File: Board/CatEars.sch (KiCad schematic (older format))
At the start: 41 parts, among them J1 Conn_01x03, J2 USB_B_Micro, J3 Conn_01x03, J31 Conn_01x01, J32 Conn_01x01, SW1 SW_Push, U1 ATSAMD21E18A-AU, U2 AP2112K-3.3

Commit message: Minor board design revision to allow more space to connect battery and easier assembly
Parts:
- removed SW1: SW_Push, Button_Switch_SMD:SW_SPST_EVQPE1, symbol Switch:SW_Push
- added 3V3, GND0: Conn_01x01, TestPoint:TestPoint_Pad_D1.0mm, symbol Connector_Generic:Conn_01x01
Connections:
- net +3V3: now also 3V3.1 (Pin_1)
- net GND: now also GND0.1 (Pin_1)
- no-connect marks 22 -> 23
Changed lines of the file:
@@
-	1    0    0    -1
-$EndComp
-$Comp
-L power:GND #PWR0103
-U 1 1 5E1A21AD
-P 5100 2350
-F 0 "#PWR0103" H 5100 2100 50  0001 C CNN
-F 1 "GND" H 5105 2177 50  0000 C CNN
-F 2 "" H 5100 2350 50  0001 C CNN
-F 3 "" H 5100 2350 50  0001 C CNN
-	1    5100 2350
 	1    0    0    -1
 $EndComp
@@
 F 3 "~" H 4650 1300 50  0001 C CNN
 	1    4650 1300
-	1    0    0    -1
-$EndComp
-$Comp
-L Switch:SW_Push SW1
-U 1 1 5E29FBEB
-P 4900 2350
-F 0 "SW1" H 4900 2635 50  0000 C CNN
-F 1 "SW_Push" H 4900 2544 50  0000 C CNN
-F 2 "Button_Switch_SMD:SW_SPST_EVQPE1" H 4900 2550 50  0001 C CNN
-F 3 "~" H 4900 2550 50  0001 C CNN
-	1    4900 2350
 	1    0    0    -1
 $EndComp
@@
 $EndComp
 Wire Wire Line
-	4350 2350 4700 2350
-Wire Wire Line
 	650  3500 650  3900
 Connection ~ 900  4050
-Connection ~ 900  3750
 Wire Wire Line
 	5300 3900 6350 3900
@@
 Wire Wire Line
 	5850 4050 6000 4050
-Connection ~ 5850 3750
 Wire Wire Line
 	6000 3750 6000 3600
@@
 $EndComp
 $Comp
-L power:+3.3V #PWR0122
-U 1 1 5E42FF29
-P 5850 3750
-F 0 "#PWR0122" H 5850 3600 50  0001 C CNN
-F 1 "+3.3V" H 5865 3923 50  0000 C CNN
-F 2 "" H 5850 3750 50  0001 C CNN
-F 3 "" H 5850 3750 50  0001 C CNN
-	1    5850 3750
-	1    0    0    -1
-$EndComp
-$Comp
 L Device:C C4
 U 1 1 5E42FF1F
@@
 Wire Wire Line
 	4200 4050 4350 4050
-Connection ~ 4200 3750
 Wire Wire Line
 	4350 3750 4350 3600
@@
 $EndComp
 $Comp
-L power:+3.3V #PWR0120
-U 1 1 5E429F5A
-P 4200 3750
-F 0 "#PWR0120" H 4200 3600 50  0001 C CNN
-F 1 "+3.3V" H 4215 3923 50  0000 C CNN
-F 2 "" H 4200 3750 50  0001 C CNN
-F 3 "" H 4200 3750 50  0001 C CNN
-	1    4200 3750
-	1    0    0    -1
-$EndComp
-$Comp
 L Device:C C3
 U 1 1 5E429F50
@@
 Wire Wire Line
 	2550 4050 2700 4050
-Connection ~ 2550 3750
 Wire Wire Line
 	2700 3750 2700 3600
@@
 $EndComp
 $Comp
-L power:+3.3V #PWR0118
-U 1 1 5E420545
-P 2550 3750
-F 0 "#PWR0118" H 2550 3600 50  0001 C CNN
-F 1 "+3.3V" H 2565 3923 50  0000 C CNN
-F 2 "" H 2550 3750 50  0001 C CNN
-F 3 "" H 2550 3750 50  0001 C CNN
-	1    2550 3750
-	1    0    0    -1
-$EndComp
-$Comp
 L Device:C C2
 U 1 1 5E42053B
@@
 $EndComp
 $Comp
-L power:+3.3V #PWR0101
-U 1 1 5E0B2653
-P 900 3750
-F 0 "#PWR0101" H 900 3600 50  0001 C CNN
-F 1 "+3.3V" H 915 3923 50  0000 C CNN
-F 2 "" H 900 3750 50  0001 C CNN
-F 3 "" H 900 3750 50  0001 C CNN
-	1    900  3750
-	1    0    0    -1
-$EndComp
-$Comp
 L Device:C C1
 U 1 1 5E0B059C
@@
 $EndComp
 $Comp
-L power:+3.3V #PWR0124
-U 1 1 5E43570B
-P 7500 3750
-F 0 "#PWR0124" H 7500 3600 50  0001 C CNN
-F 1 "+3.3V" H 7515 3923 50  0000 C CNN
-F 2 "" H 7500 3750 50  0001 C CNN
-F 3 "" H 7500 3750 50  0001 C CNN
-	1    7500 3750
-	1    0    0    -1
-$EndComp
-$Comp
 L power:GND #PWR0125
 U 1 1 5E435715
@@
 Wire Wire Line
 	7650 3750 7650 3600
-Connection ~ 7500 3750
 Wire Wire Line
 	7500 4050 7650 4050
@@
 	6850 3000 8200 3000
 NoConn ~ 6350 6950
+$Comp
+L power:+3V3 #PWR0101
+U 1 1 5E5C8317
+P 7500 3750
+F 0 "#PWR0101" H 7500 3600 50  0001 C CNN
+F 1 "+3V3" H 7515 3923 50  0000 C CNN
+F 2 "" H 7500 3750 50  0001 C CNN
+F 3 "" H 7500 3750 50  0001 C CNN
+	1    7500 3750
+	1    0    0    -1
+$EndComp
+Connection ~ 7500 3750
+$Comp
+L power:+3V3 #PWR0118
+U 1 1 5E5C8983
+P 5850 3750
+F 0 "#PWR0118" H 5850 3600 50  0001 C CNN
+F 1 "+3V3" H 5865 3923 50  0000 C CNN
+F 2 "" H 5850 3750 50  0001 C CNN
+F 3 "" H 5850 3750 50  0001 C CNN
+	1    5850 3750
+	1    0    0    -1
+$EndComp
+Connection ~ 5850 3750
+$Comp
+L power:+3V3 #PWR0120
+U 1 1 5E5C8C12
+P 4200 3750
+F 0 "#PWR0120" H 4200 3600 50  0001 C CNN
+F 1 "+3V3" H 4215 3923 50  0000 C CNN
+F 2 "" H 4200 3750 50  0001 C CNN
+F 3 "" H 4200 3750 50  0001 C CNN
+	1    4200 3750
+	1    0    0    -1
+$EndComp
+Connection ~ 4200 3750
+$Comp
+L power:+3V3 #PWR0122
+U 1 1 5E5C9834
+P 2550 3750
+F 0 "#PWR0122" H 2550 3600 50  0001 C CNN
+F 1 "+3V3" H 2565 3923 50  0000 C CNN
+F 2 "" H 2550 3750 50  0001 C CNN
+F 3 "" H 2550 3750 50  0001 C CNN
+	1    2550 3750
+	1    0    0    -1
+$EndComp
+Connection ~ 2550 3750
+$Comp
+L power:+3V3 #PWR0124
+U 1 1 5E5C9D8C
+P 900 3750
+F 0 "#PWR0124" H 900 3600 50  0001 C CNN
+F 1 "+3V3" H 915 3923 50  0000 C CNN
+F 2 "" H 900 3750 50  0001 C CNN
+F 3 "" H 900 3750 50  0001 C CNN
+	1    900  3750
+	1    0    0    -1
+$EndComp
+Connection ~ 900  3750
+$Comp
+L Connector_Generic:Conn_01x01 GND0
+U 1 1 5E5CA3E1
+P 1400 2000
+F 0 "GND0" H 1480 2042 50  0000 L CNN
+F 1 "Conn_01x01" H 1480 1951 50  0000 L CNN
+F 2 "TestPoint:TestPoint_Pad_D1.0mm" H 1400 2000 50  0001 C CNN
+F 3 "~" H 1400 2000 50  0001 C CNN
+	1    1400 2000
+	1    0    0    -1
+$EndComp
+$Comp
+L Connector_Generic:Conn_01x01 3V3
+U 1 1 5E5CA8D8
+P 1400 1650
+F 0 "3V3" H 1480 1692 50  0000 L CNN
+F 1 "Conn_01x01" H 1480 1601 50  0000 L CNN
+F 2 "TestPoint:TestPoint_Pad_D1.0mm" H 1400 1650 50  0001 C CNN
+F 3 "~" H 1400 1650 50  0001 C CNN
+	1    1400 1650
+	1    0    0    -1
+$EndComp
+$Comp
+L power:+3V3 #PWR0126
+U 1 1 5E5CAB98
+P 1200 1650
+F 0 "#PWR0126" H 1200 1500 50  0001 C CNN
+F 1 "+3V3" H 1215 1823 50  0000 C CNN
+F 2 "" H 1200 1650 50  0001 C CNN
+F 3 "" H 1200 1650 50  0001 C CNN
+	1    1200 1650
+	1    0    0    -1
+$EndComp
+$Comp
+L power:GND #PWR0127
+U 1 1 5E5CB0E5
+P 1200 2000
+F 0 "#PWR0127" H 1200 1750 50  0001 C CNN
+F 1 "GND" H 1205 1827 50  0000 C CNN
+F 2 "" H 1200 2000 50  0001 C CNN
+F 3 "" H 1200 2000 50  0001 C CNN
+	1    1200 2000
+	1    0    0    -1
+$EndComp
+NoConn ~ 4350 2350
 $EndSCHEMATC

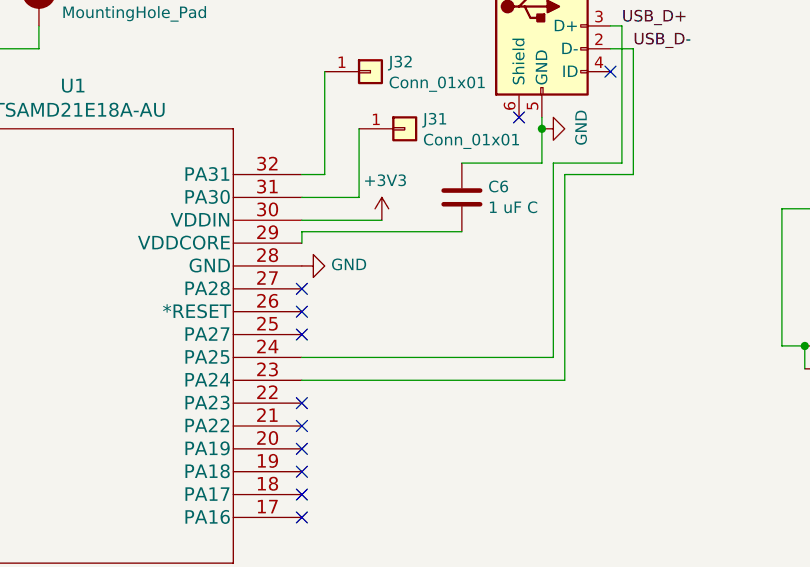
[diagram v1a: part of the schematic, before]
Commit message: New OSH Park link, rev notes, restored reset
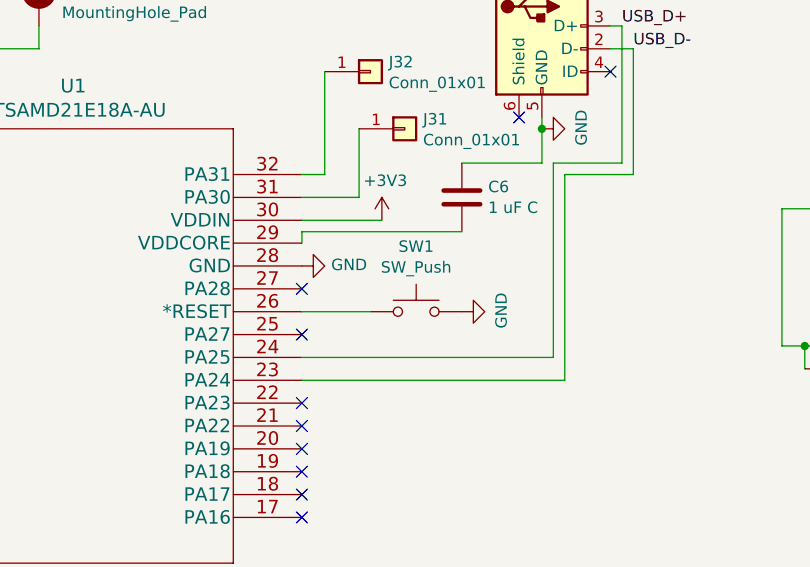
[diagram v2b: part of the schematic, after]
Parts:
- added SW1: SW_Push, Button_Switch_SMD:SW_SPST_TL3342, symbol Switch:SW_Push
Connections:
- net GND: now also SW1.2
- net at U1.26 (*RESET): now also SW1.1
- no-connect marks 23 -> 22
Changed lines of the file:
@@
 	1    0    0    -1
 $EndComp
-NoConn ~ 4350 2350
+$Comp
+L Switch:SW_Push SW1
+U 1 1 5E5D524B
+P 4850 2350
+F 0 "SW1" H 4850 2635 50  0000 C CNN
+F 1 "SW_Push" H 4850 2544 50  0000 C CNN
+F 2 "Button_Switch_SMD:SW_SPST_TL3342" H 4850 2550 50  0001 C CNN
+F 3 "~" H 4850 2550 50  0001 C CNN
+	1    4850 2350
+	1    0    0    -1
+$EndComp
+Wire Wire Line
+	4350 2350 4650 2350
+$Comp
+L power:GND #PWR0103
+U 1 1 5E5DBFAB
+P 5050 2350
+F 0 "#PWR0103" H 5050 2100 50  0001 C CNN
+F 1 "GND" H 5055 2177 50  0000 C CNN
+F 2 "" H 5050 2350 50  0001 C CNN
+F 3 "" H 5050 2350 50  0001 C CNN
+	1    5050 2350
+	0    -1   -1   0
+$EndComp
 $EndSCHEMATC
